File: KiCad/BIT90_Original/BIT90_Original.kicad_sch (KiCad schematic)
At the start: 0 parts

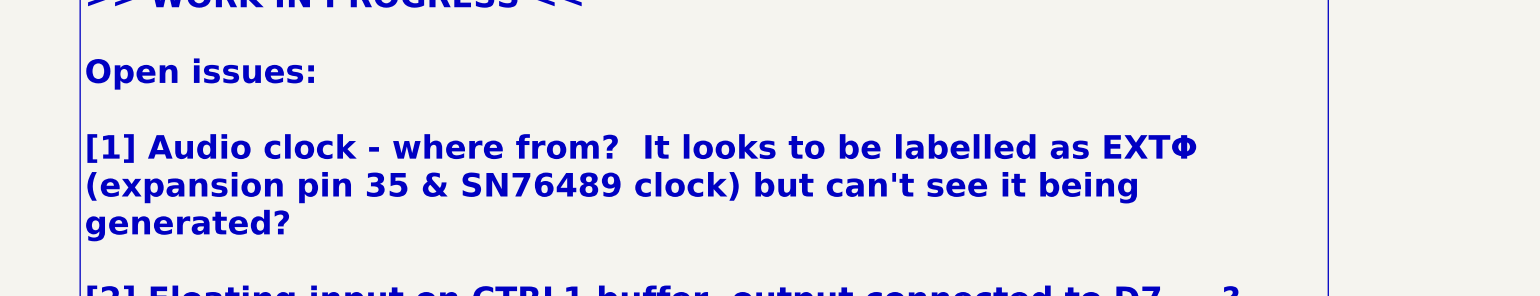
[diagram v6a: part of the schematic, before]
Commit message: Resolved audio clock signal
Marked as EXTΦ on BIT90 schematic, generated via resistor from CPUΦ
Renamed it as AUDΦ so it's a bit clearer
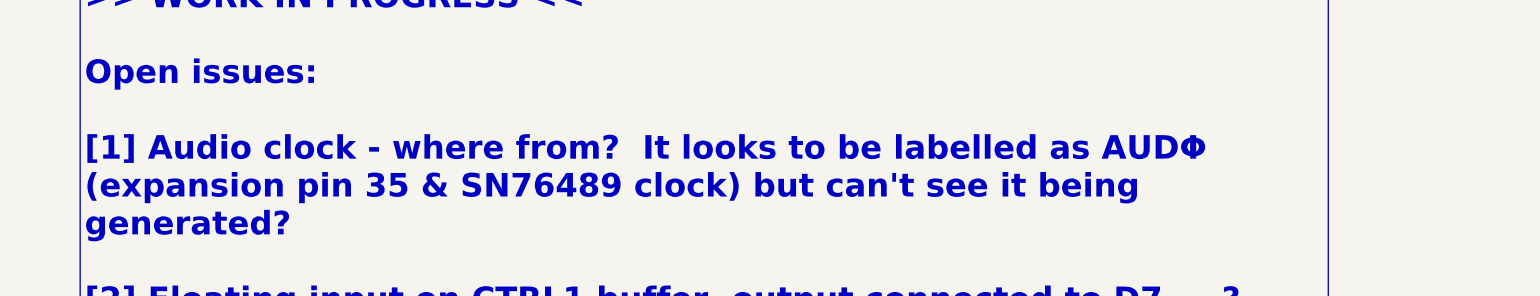
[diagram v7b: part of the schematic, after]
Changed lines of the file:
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@@
 		(comment 4 "Based on original schematics from BIT Corporation (普澤有限公司)")
 	)
-	(text_box ">> WORK IN PROGRESS <<\n\nOpen issues:\n\n[1] Audio clock - where from?  It looks to be labelled as EXTΦ (expansion pin 35 & SN76489 clock) but can't see it being generated?\n\n[2] Floating input on CTRL1 buffer, output connected to D7 ... ?"
+	(text_box ">> WORK IN PROGRESS <<\n\nOpen issues:\n\n[1] Audio clock - where from?  It looks to be labelled as AUDΦ (expansion pin 35 & SN76489 clock) but can't see it being generated?\n\n[2] Floating input on CTRL1 buffer, output connected to D7 ... ?"
 		(exclude_from_sim no)
 		(at 121.92 100.33 0)
